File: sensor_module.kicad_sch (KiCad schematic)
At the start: 6 parts, among them U12 REF3025, U13 MCP3208, U14 INA333xxDGK, U6 M24C02-WMN, U7 TPS22929D, U8 REF3040

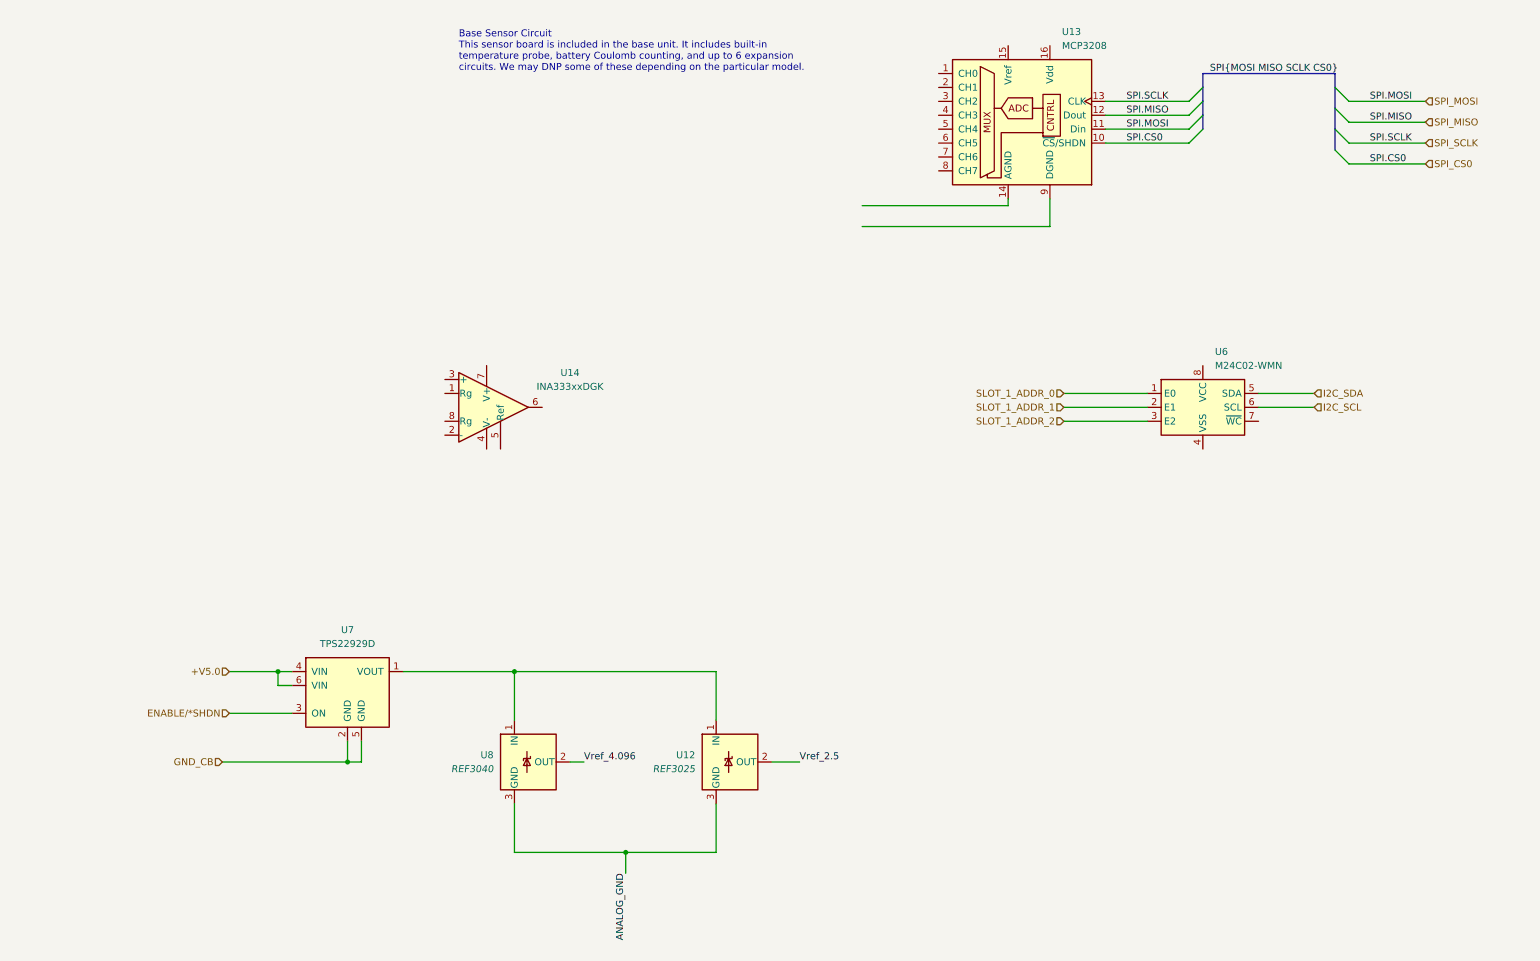
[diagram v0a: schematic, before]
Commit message: Sensor board basic updates
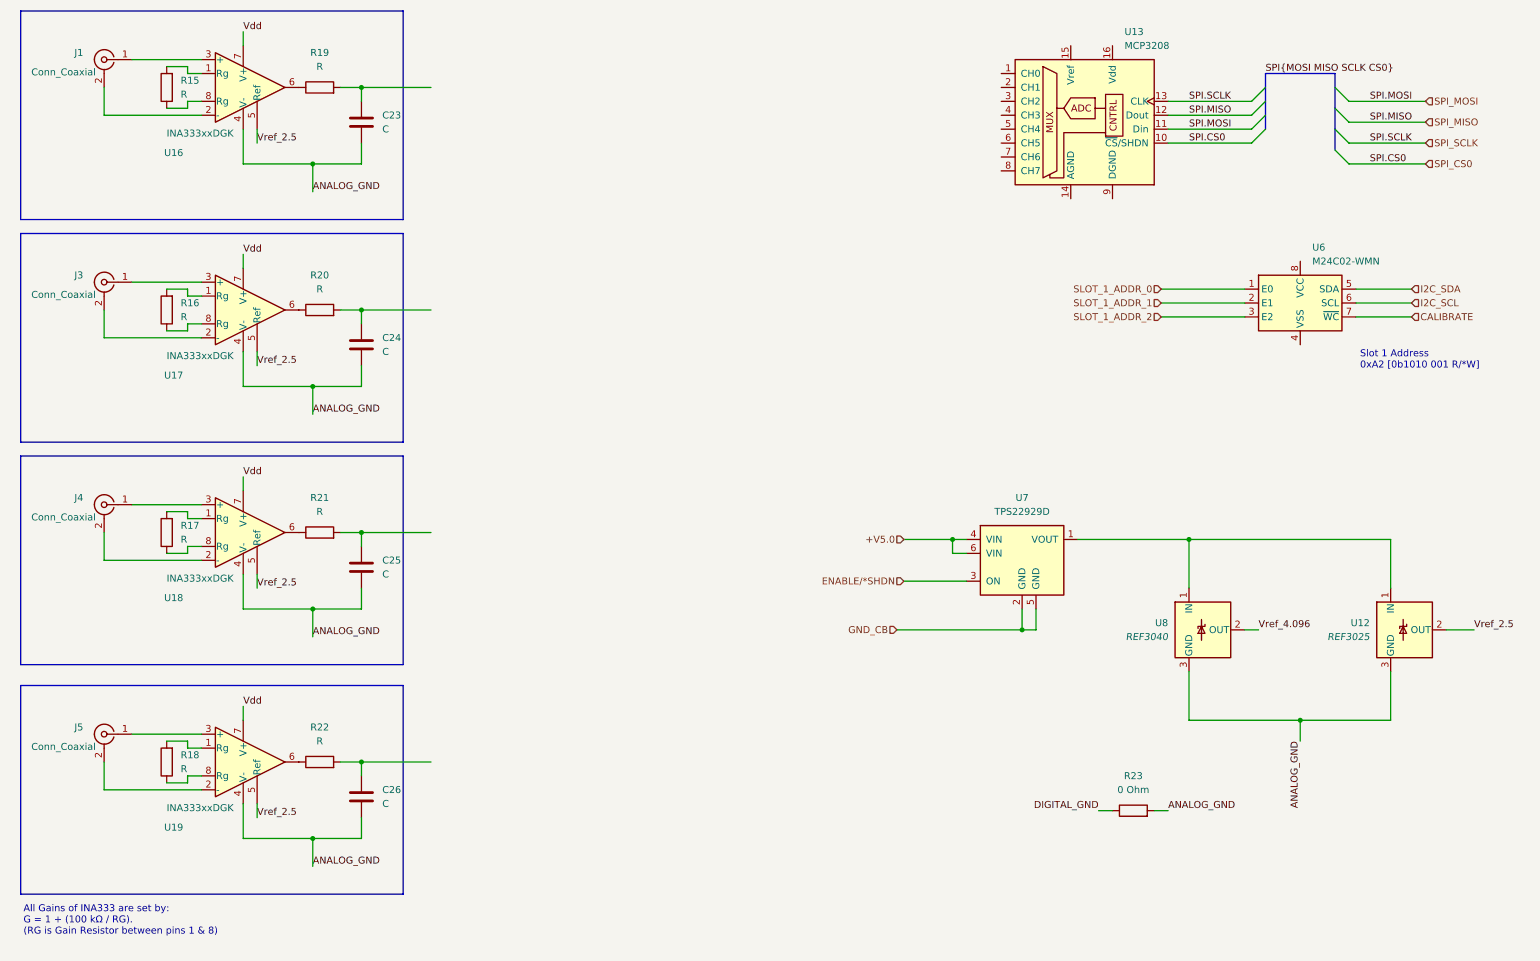
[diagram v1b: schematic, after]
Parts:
- removed U14: INA333xxDGK, Package_SO:VSSOP-8_3x3mm_P0.65mm, symbol Amplifier_Instrumentation:INA333xxDGK
- added C23, C24, C25, C26: C, symbol Device:C
- added J1, J3, J4, J5: Conn_Coaxial, symbol Connector:Conn_Coaxial
- added R15, R16, R17, R18, R19, R20, R21, R22: R, symbol Device:R
- added R23: 0 Ohm, symbol Device:R
- added U16, U17, U18, U19: INA333xxDGK, Package_SO:VSSOP-8_3x3mm_P0.65mm, symbol Amplifier_Instrumentation:INA333xxDGK
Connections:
- net ANALOG_GND: now also C23.2, C24.2, C25.2, C26.2, R23.2, U16.4 (V-), U17.4 (V-), U18.4 (V-), U19.4 (V-)
- net Vref_2.5: now also U16.5 (Ref), U17.5 (Ref), U18.5 (Ref), U19.5 (Ref)
- net CALIBRATE: now reaches U6.7 (~{WC})
- new net: R16.1, U17.8 (Rg)
- new net: R16.2, U17.1 (Rg)
- new net: C26.1, R22.2
- new net: R19.1, U16.6
- new net: C23.1, R19.2
- new net: R21.1, U18.6
- new net: C25.1, R21.2
- new net: J4.1 (In), U18.3 (+)
- new net: J4.2 (Ext), U18.2 (-)
- new net: R17.2, U18.1 (Rg)
- new net: R17.1, U18.8 (Rg)
- new net: R18.2, U19.1 (Rg)
- new net: J5.2 (Ext), U19.2 (-)
- new net: J5.1 (In), U19.3 (+)
- new net: R22.1, U19.6
- new net: R18.1, U19.8 (Rg)
- new net: J1.1 (In), U16.3 (+)
- new net: J1.2 (Ext), U16.2 (-)
- new net: R15.1, U16.8 (Rg)
- new net: R15.2, U16.1 (Rg)
- new net: C24.1, R20.2
- new net: J3.1 (In), U17.3 (+)
- new net: J3.2 (Ext), U17.2 (-)
- new net: R20.1, U17.6
- new net DIGITAL_GND: R23.1
- new net Vdd: U16.7 (V+), U17.7 (V+), U18.7 (V+), U19.7 (V+)
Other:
- note added: "All Gains of INA333 are set by: G = 1 + (100 kΩ / RG). (RG is Gain Resistor between pins 1 & 8)"
- note added: "Slot 1 Address 0xA2 [0b1010 001 R/*W]"
- note removed: "Base Sensor Circuit This sensor board is included in the base unit. It includes built-in temperature probe, battery Coulomb counting, and up to 6 expansion circuits. We may DNP some of these depending on the particular model."
- moved on the sheet: U12, U13, U6, U7, U8
